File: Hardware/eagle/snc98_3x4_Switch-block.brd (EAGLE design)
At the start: 56.4 x 83.2 mm, 67 parts

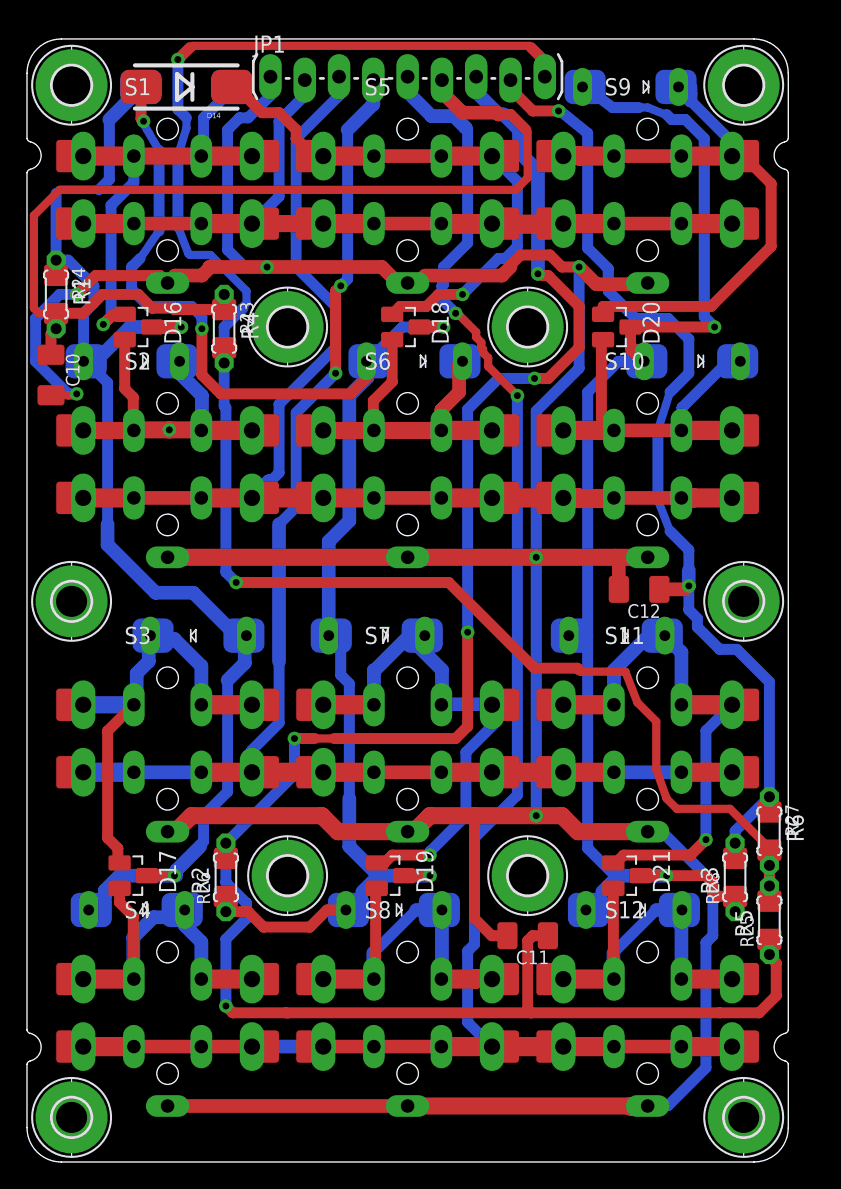
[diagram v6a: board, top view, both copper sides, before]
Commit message: PCB - add Tear Drop
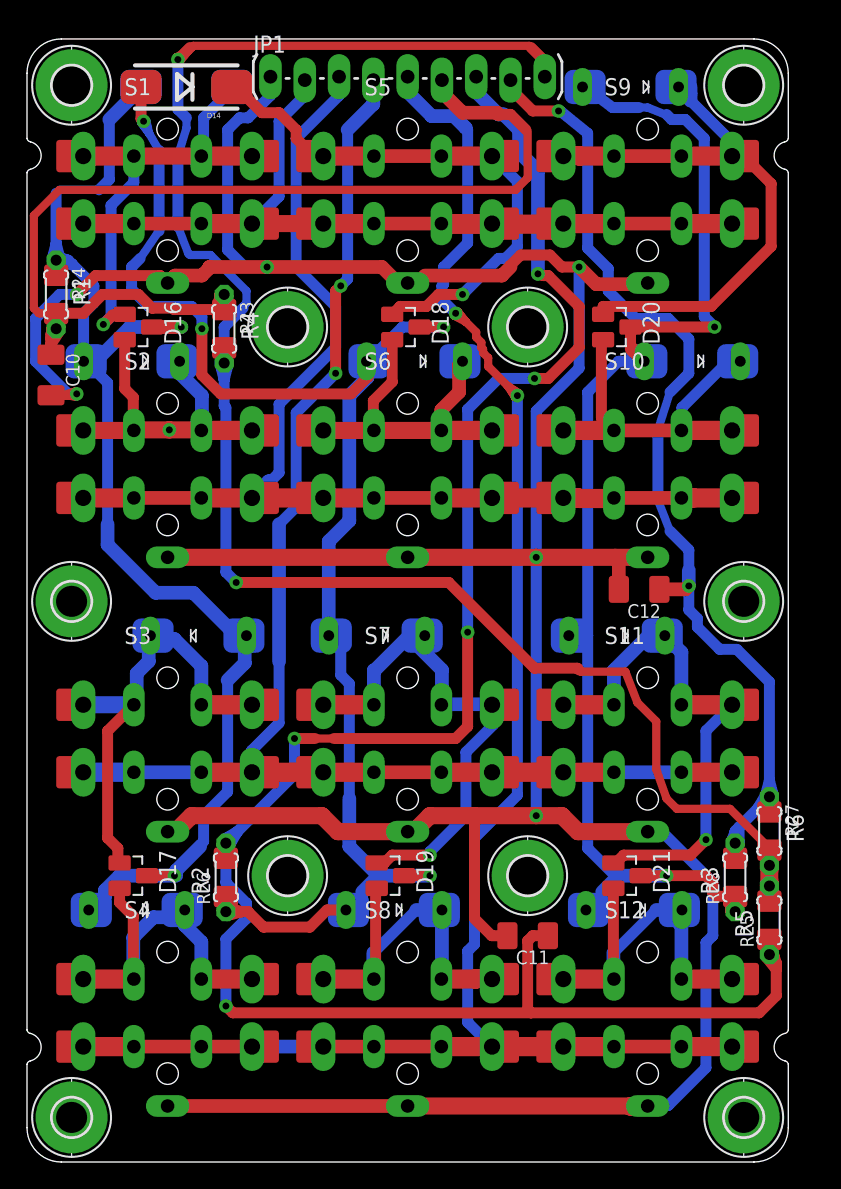
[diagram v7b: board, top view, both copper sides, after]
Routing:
- net AREF: track 128.7 -> 172.8 mm
- net A3: track 75.0 -> 94.5 mm
- net A2: track 149.2 -> 167.4 mm
- net A1: track 76.7 -> 92.0 mm
- net A_1: track 99.5 -> 111.8 mm
- net A_2: track 112.0 -> 123.5 mm
- net C4: track 133.3 -> 141.8 mm
- net A_3: track 94.0 -> 99.1 mm
- net GND: track 268.9 -> 273.2 mm

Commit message: Gerber file added
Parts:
- added R10, R11, R9: 27k, rcl:M0805
- added R33, R7, R8: 6k8, rcl:M0805
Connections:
- net A1: now also R33.2, R9.1
- net A2: now also R10.1, R7.2
- net A3: now also R11.1, R8.2
- net AREF: now also R10.2, R11.2, R9.2
- net A_1: now also R33.1
- net A_2: now also R7.1
- net A_3: now also R8.1
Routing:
- net AREF: track 172.8 -> 177.4 mm
- net A3: track 94.5 -> 97.5 mm
- net A2: track 167.4 -> 170.4 mm
- net A1: track 92.0 -> 95.0 mm
- net A_3: track 99.1 -> 100.6 mm
- net A_2: track 123.5 -> 125.0 mm
- net A_1: track 111.8 -> 113.3 mm
